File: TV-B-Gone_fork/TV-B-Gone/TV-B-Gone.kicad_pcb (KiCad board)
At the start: 2 copper layers, 23 parts, among them J1 AVR-ISP-6, Q1 2N3904, Q2 2N3904, Q3 BC557, Q4 2N3904, Q5 2N3904, U1 ATtiny85V-10PU, Y1 8Mhz

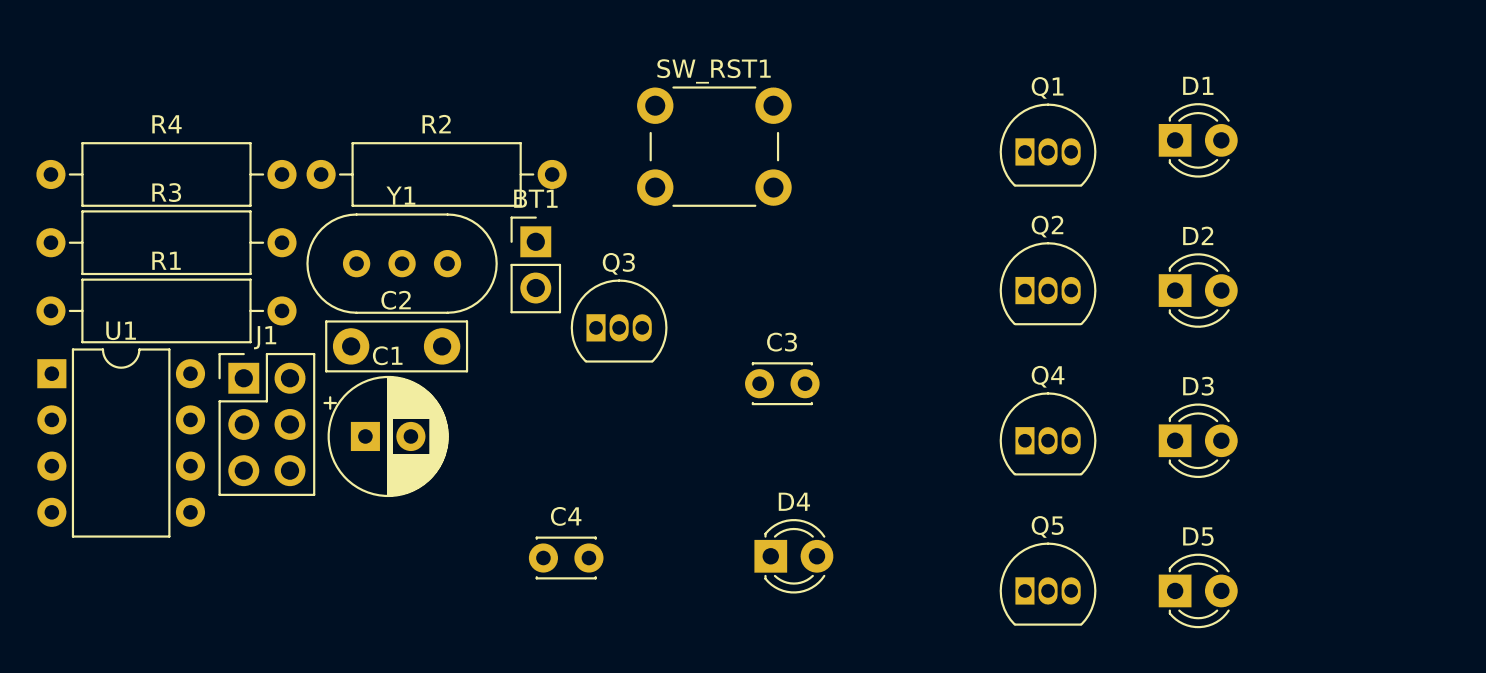
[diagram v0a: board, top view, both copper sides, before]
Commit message: Agregado libreria externa para algunos capacitores.
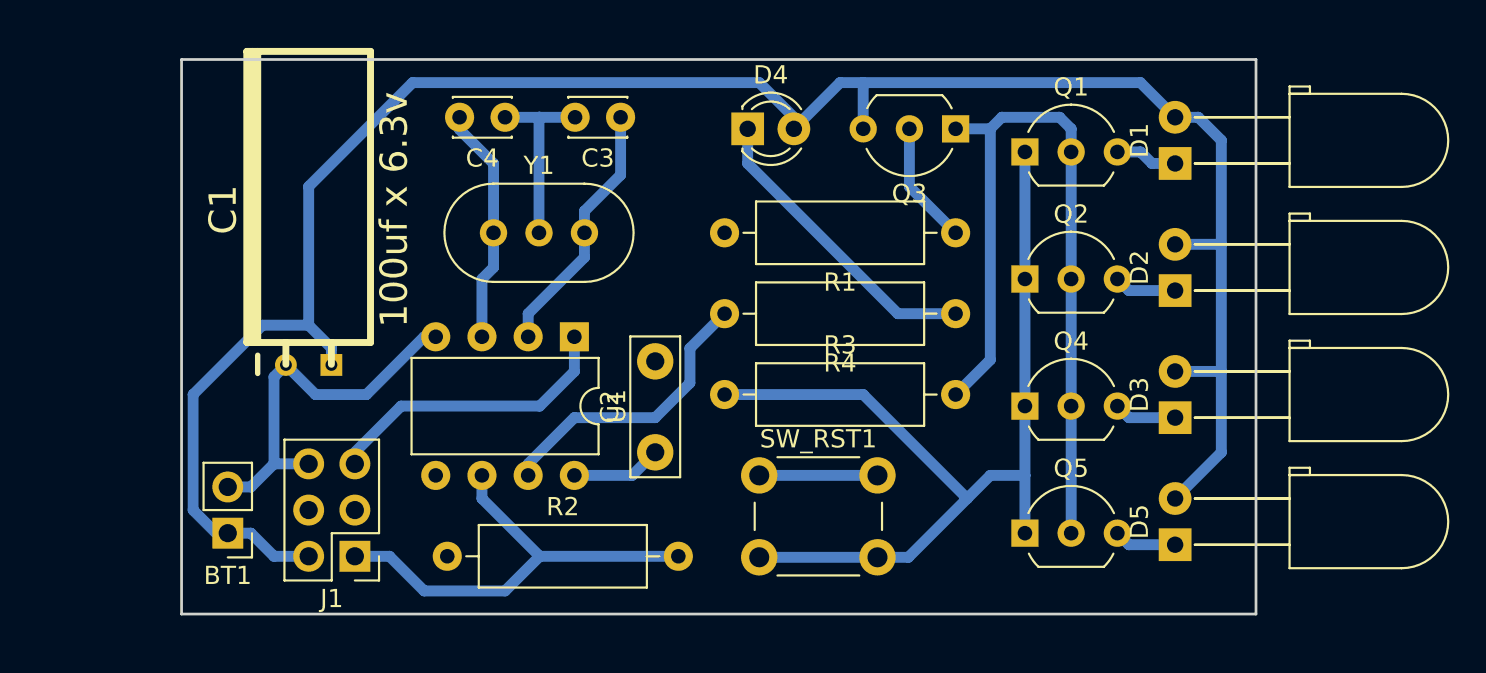
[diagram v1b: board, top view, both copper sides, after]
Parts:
- C1: footprint Capacitor_THT:CP_Radial_D6.3mm_P2.50mm -> w_capacitors:CP_6.3x15mm_hor
- D1, D2, D3, D5: footprint LED_THT:LED_D3.0mm_IRBlack -> LED_THT:LED_D5.0mm_Horizontal_O6.35mm_Z3.0mm
- Q1, Q2, Q3, Q4, Q5: footprint Package_TO_SOT_THT:TO-92_Inline -> Package_TO_SOT_THT:TO-92_Inline_Wide
- moved R4 50.3 mm to (99.7, 34.9), turned to 180 degrees
- moved R1 49.9 mm to (99.7, 30.5), turned to 180 degrees
- moved R3 38.0 mm to (87.0, 39.4)
- moved U1 28.8 mm to (78.7, 36.2), turned to 270 degrees
- moved C4 24.3 mm to (74.9, 24.1), turned to 180 degrees
- moved D4 23.5 mm to (88.3, 24.8)
- moved BT1 23.3 mm to (59.7, 47.0), turned to 180 degrees
- moved Q3 22.6 mm to (99.7, 24.8), turned to 180 degrees
- moved R2 22.1 mm to (71.8, 48.3)
- moved SW_RST1 21.1 mm to (88.9, 43.8)
- moved C2 17.7 mm to (83.2, 42.5), turned to 90 degrees
- moved C3 16.5 mm to (81.3, 24.1), turned to 180 degrees
- moved C1 12.8 mm to (64.1, 29.2), turned to 90 degrees
- moved J1 11.5 mm to (66.7, 48.3), turned to 180 degrees
- moved Y1 7.71 mm to (74.3, 30.5)
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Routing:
- net VCC: track 0.00 -> 121.7 mm
- net GND: track 0.00 -> 84.3 mm
- net Net-(Q1-Pad2): track 0.00 -> 44.5 mm
- net /MISO: track 0.00 -> 25.1 mm
- net /RST: track 0.00 -> 22.9 mm
- net Net-(D4-Pad1): track 0.00 -> 16.8 mm
- net /SCK: track 0.00 -> 16.0 mm
- net Net-(C3-Pad1): track 0.00 -> 14.2 mm
- net Net-(C4-Pad2): track 0.00 -> 13.1 mm
- net Net-(Q3-Pad2): track 0.00 -> 6.77 mm
- net Net-(D1-Pad1): track 0.00 -> 3.44 mm
- net Net-(D5-Pad1): track 0.00 -> 3.44 mm
- net Net-(D3-Pad1): track 0.00 -> 3.44 mm
- net Net-(D2-Pad1): track 0.00 -> 3.44 mm
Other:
- board outline added: 59.1 x 30.5 mm
- net class Default: clearance 0.2 -> 0.3; trace_width 0.25 -> 0.6
- rule trace_clearance: 0.2 -> 0.3

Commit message: Ruteando. Asignación modelo 3D capacitor.
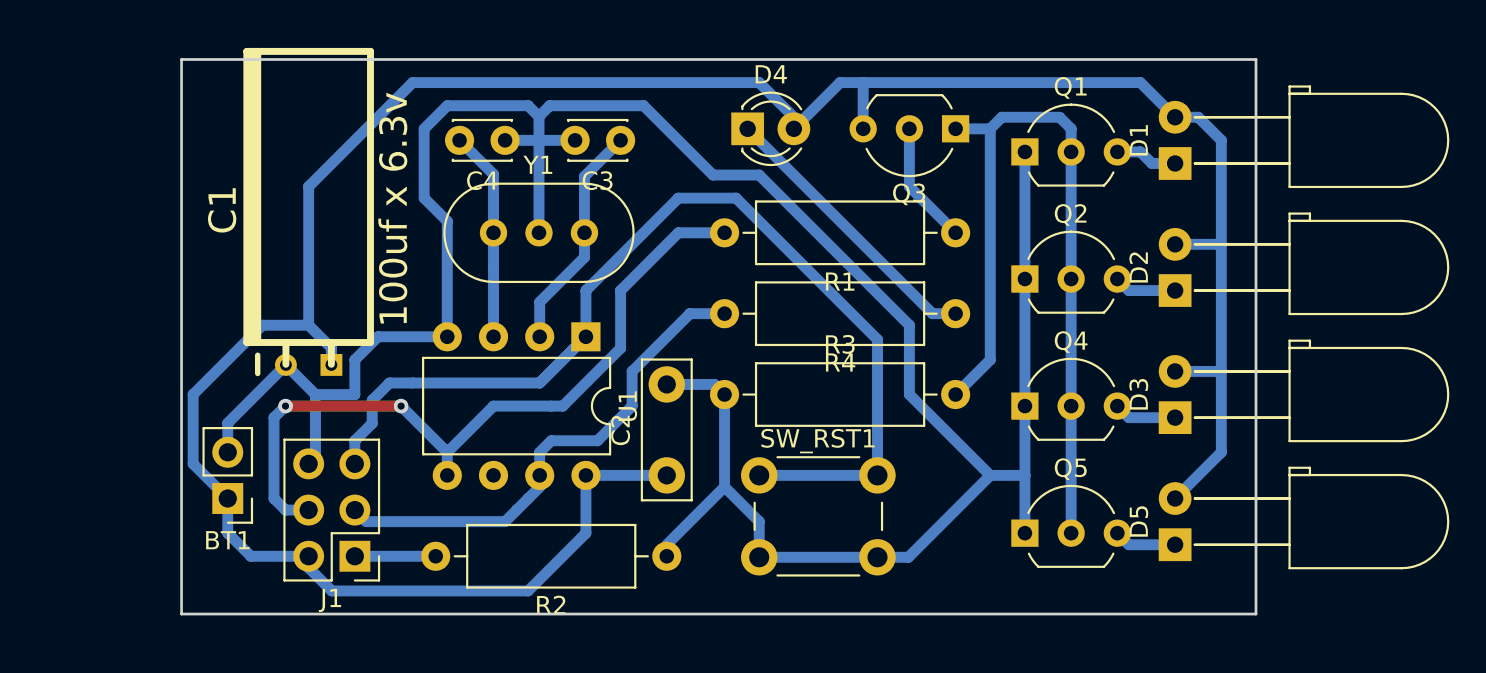
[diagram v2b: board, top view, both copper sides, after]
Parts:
- moved R2 12.1 mm to (83.8, 48.3), turned to 180 degrees
- moved BT1 1.91 mm to (59.7, 45.1)
- moved C2 1.42 mm to (83.8, 43.8)
- moved C3 1.27 mm to (81.3, 25.4)
- moved C4 1.27 mm to (74.9, 25.4)
- moved U1 0.64 mm to (79.4, 36.2)
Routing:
- net GND: track 84.3 -> 142.1 mm
- net /MOSI: track 0.00 -> 40.8 mm, vias 0 -> 2
- net /RST: track 22.9 -> 57.6 mm
- net /MISO: track 25.1 -> 4.45 mm
- net VCC: track 121.7 -> 141.0 mm
- net /SCK: track 16.0 -> 27.5 mm
- net Net-(C4-Pad2): track 13.1 -> 11.6 mm
- net Net-(C3-Pad1): track 14.2 -> 12.6 mm
- net Net-(D4-Pad1): track 16.8 -> 15.6 mm

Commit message: Ruteado terminado. Agregado de copia del software para la versión de hard.
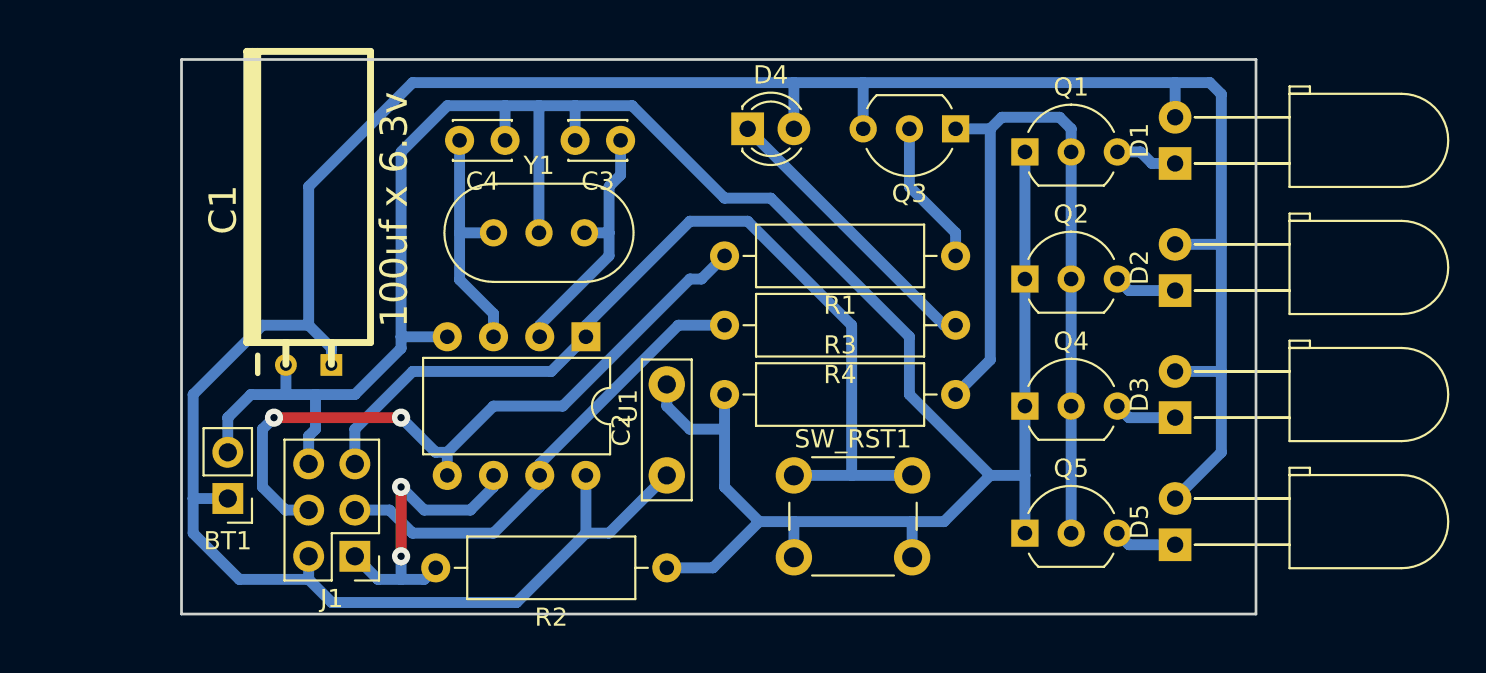
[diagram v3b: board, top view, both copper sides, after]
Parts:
- moved SW_RST1 1.91 mm to (90.8, 43.8)
- moved R1 1.27 mm to (99.7, 31.8)
- moved R2 0.64 mm to (83.8, 48.9)
- moved R4 0.64 mm to (99.7, 35.6)
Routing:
- net /MISO: track 4.45 -> 17.1 mm, vias 0 -> 2
- net VCC: track 141.0 -> 150.9 mm
- net /RST: track 57.6 -> 51.4 mm
- net GND: track 142.1 -> 145.8 mm
- net /MOSI: track 40.8 -> 38.4 mm
- net Net-(C4-Pad2): track 11.6 -> 13.4 mm
- net Net-(C3-Pad1): track 12.6 -> 14.0 mm
- net Net-(Q3-Pad2): track 6.77 -> 8.04 mm
- net /SCK: track 27.5 -> 26.3 mm
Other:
- net class Default: via_dia 0.8 -> 1

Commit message: Agrandado de vias. Ajustes a clearance de 0.6 mm.
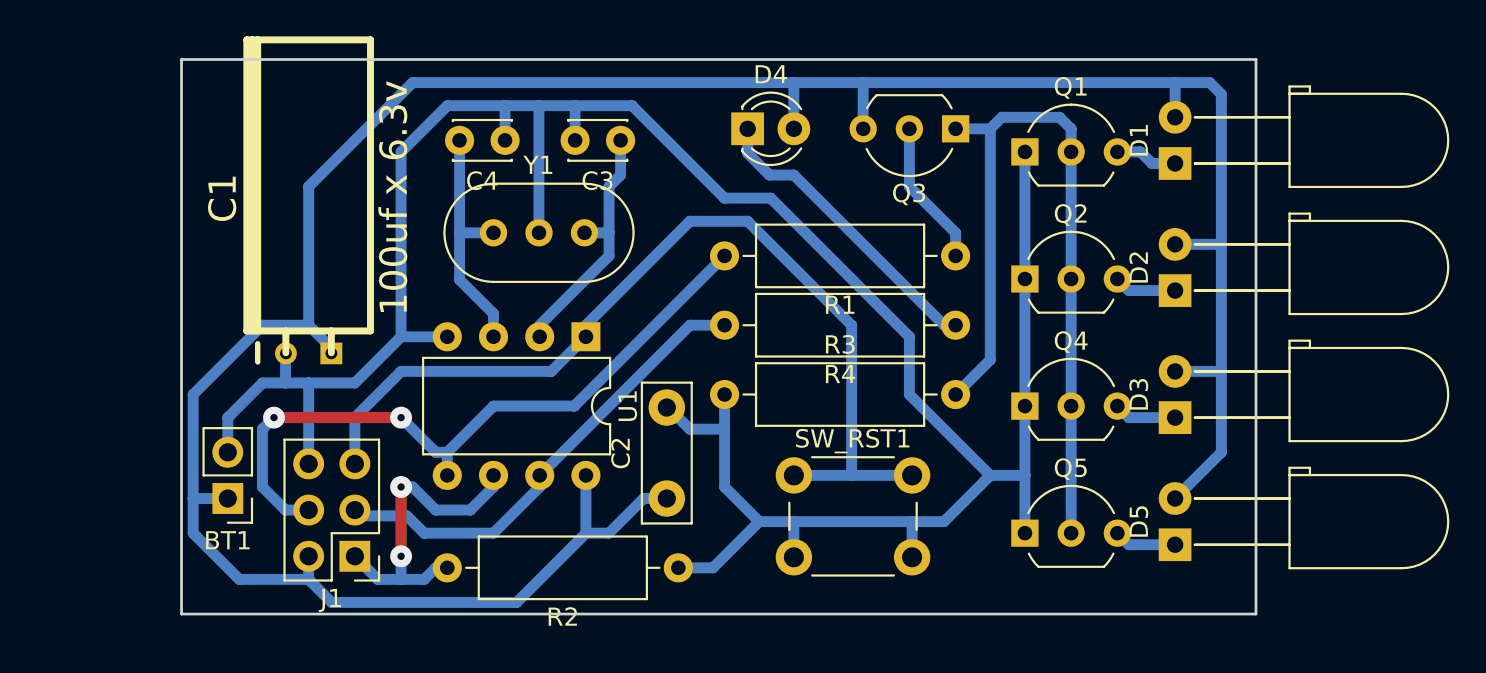
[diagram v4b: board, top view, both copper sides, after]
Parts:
- moved C2 1.27 mm to (83.8, 45.1)
- moved R2 0.64 mm to (84.5, 48.9)
- moved C1 0.64 mm to (64.1, 28.6)
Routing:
- net GND: track 145.8 -> 144.1 mm
- net VCC: track 150.9 -> 149.7 mm
- net Net-(D4-Pad1): track 15.9 -> 16.7 mm
- net /MISO: track 17.1 -> 17.7 mm
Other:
- net class Default: clearance 0.3 -> 0.6; via_dia 1 -> 1.2
- rule trace_clearance: 0.3 -> 0.6

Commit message: Ajuste de vias a 1.6 mm, taladro 0.75 mm. Cambio de huella de algunos capacitores. Ajuste tamaño de pads algunos componentes. Eliminación de librerias de 3ros.
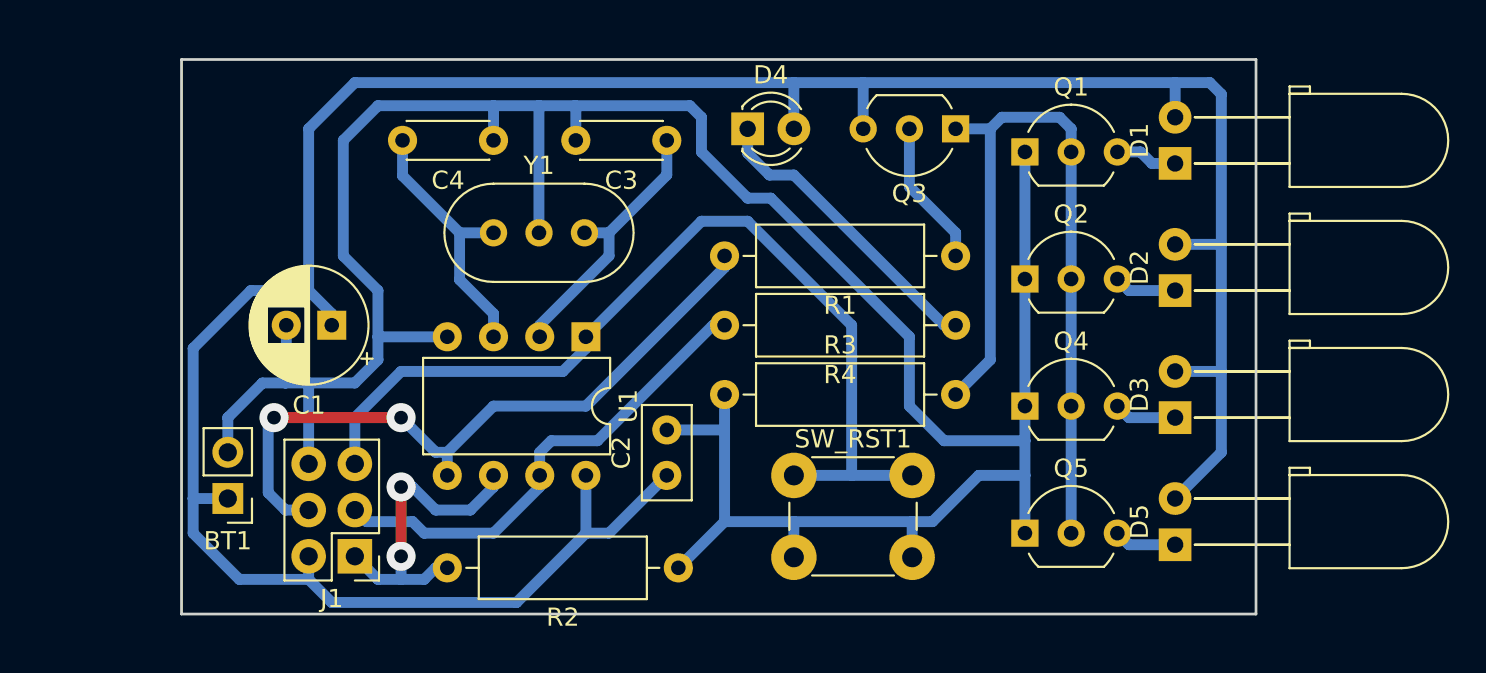
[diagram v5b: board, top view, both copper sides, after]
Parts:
- C1: footprint w_capacitors:CP_6.3x15mm_hor -> Capacitor_THT:CP_Radial_D6.3mm_P2.50mm
- C2: footprint Capacitor_THT:C_Disc_D7.5mm_W2.5mm_P5.00mm -> Capacitor_THT:C_Disc_D5.0mm_W2.5mm_P2.50mm
- C3, C4: footprint Capacitor_THT:C_Disc_D3.0mm_W2.0mm_P2.50mm -> Capacitor_THT:C_Disc_D4.3mm_W1.9mm_P5.00mm
- moved C1 7.10 mm to (65.4, 35.6), turned to 180 degrees
- moved C3 2.54 mm to (83.8, 25.4)
- moved C2 1.27 mm to (83.8, 43.8)
- moved C4 0.64 mm to (74.3, 25.4)
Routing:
- net GND: track 144.1 -> 152.0 mm
- net VCC: track 149.7 -> 152.8 mm
- net Net-(C4-Pad2): track 13.4 -> 14.7 mm
- net Net-(C3-Pad1): track 14.0 -> 15.0 mm
- net /SCK: track 26.0 -> 26.7 mm
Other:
- net class Default: via_dia 1.2 -> 1.6; via_drill 0.4 -> 0.75

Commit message: Cambio huellas resistencias y ajuste de pistas.
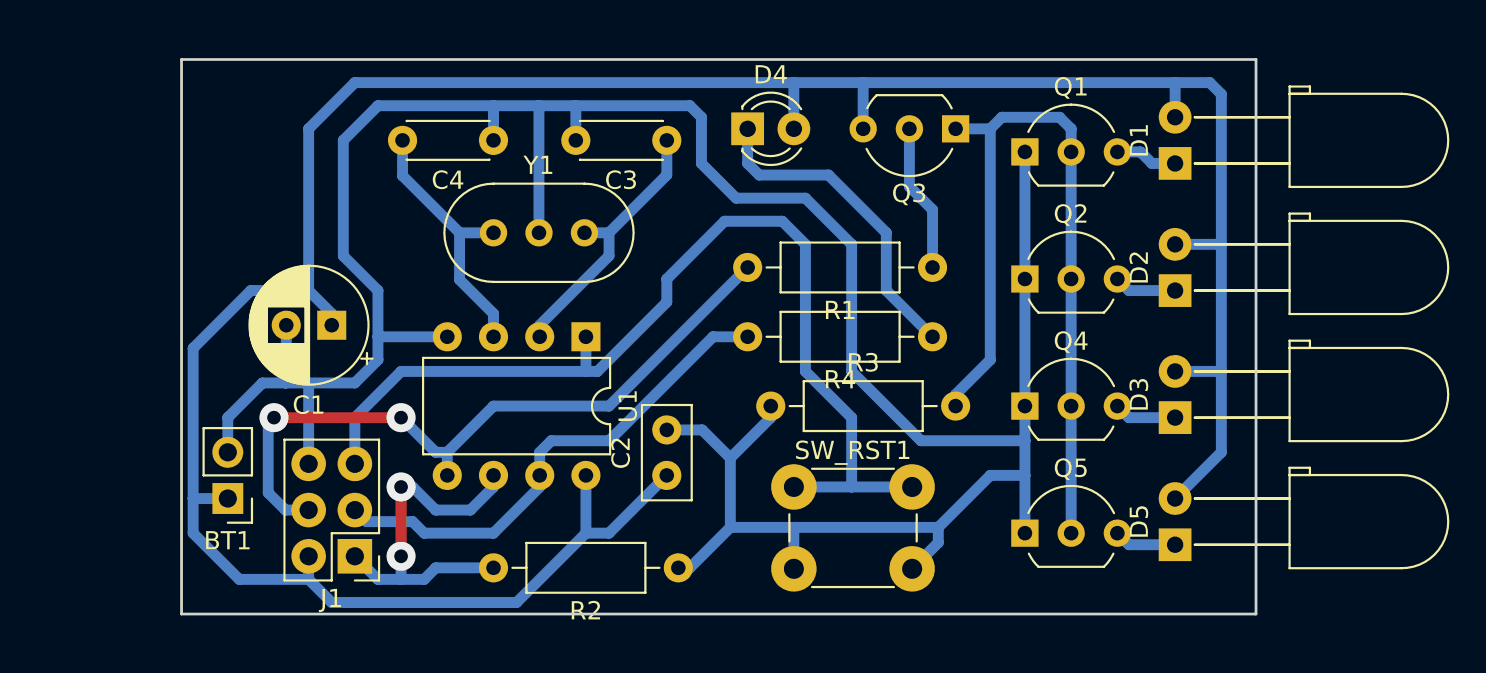
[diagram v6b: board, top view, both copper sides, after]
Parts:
- R1, R2, R3, R4: footprint Resistor_THT:R_Axial_DIN0309_L9.0mm_D3.2mm_P12.70mm_Horizontal -> Resistor_THT:R_Axial_DIN0207_L6.3mm_D2.5mm_P10.16mm_Horizontal
- moved R3 2.62 mm to (89.5, 40.0)
- moved R1 1.42 mm to (98.4, 32.4)
- moved R4 1.42 mm to (98.4, 36.2)
- moved SW_RST1 0.64 mm to (90.8, 44.5)
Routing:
- net GND: track 152.0 -> 157.0 mm
- net /RST: track 51.8 -> 55.8 mm
- net /MISO: track 17.7 -> 20.3 mm
- net Net-(D4-Pad1): track 16.7 -> 17.9 mm
- net /SCK: track 26.7 -> 27.7 mm
- net Net-(Q1-Pad2): track 44.5 -> 45.1 mm
- net /MOSI: track 38.5 -> 39.2 mm
